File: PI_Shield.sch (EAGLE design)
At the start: 74 parts, among them J10 T2I, J11 T2I, J12 T2I, J13 DF13-4P-1.25DSA, J14 DF13-4P-1.25DSA, J15 DF13-4P-1.25DSA, J16 T2I5P, Q1 220mA/50V/3.5Ω, Q2 220mA/50V/3.5Ω, Q3 220mA/50V/3.5Ω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

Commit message: General routing complete
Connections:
- removed net DI: U$8.GPIO6
- removed net DI3: U$8.GPIO21
- new net 3VO_1: U$4.3VO
- new net 3VO_2: U$5.3VO
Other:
- moved on the sheet: C13
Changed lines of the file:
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@@
 <?xml version="1.0" encoding="utf-8"?>
 <!DOCTYPE eagle SYSTEM "eagle.dtd">
-<eagle version="9.6.2">
+<eagle version="9.5.2">
 <drawing>
 <settings>
@@
 <attribute name="VALUE" x="193.04" y="68.58" size="1.778" layer="96"/>
 </instance>
-<instance part="C13" gate="G$1" x="238.76" y="160.02" smashed="yes">
-<attribute name="NAME" x="240.284" y="162.941" size="1.778" layer="95" font="vector"/>
-<attribute name="VALUE" x="240.284" y="157.861" size="1.778" layer="96" font="vector"/>
+<instance part="C13" gate="G$1" x="238.76" y="162.56" smashed="yes">
+<attribute name="NAME" x="240.284" y="165.481" size="1.778" layer="95" font="vector"/>
+<attribute name="VALUE" x="240.284" y="160.401" size="1.778" layer="96" font="vector"/>
 </instance>
 <instance part="J1" gate="G$1" x="236.22" y="66.04" smashed="yes">
@@
 <attribute name="VALUE" x="231.14" y="83.82" size="1.778" layer="96"/>
 </instance>
-<instance part="GND28" gate="1" x="238.76" y="152.4" smashed="yes">
-<attribute name="VALUE" x="236.22" y="149.86" size="1.778" layer="96"/>
+<instance part="GND28" gate="1" x="238.76" y="154.94" smashed="yes">
+<attribute name="VALUE" x="236.22" y="152.4" size="1.778" layer="96"/>
 </instance>
 <instance part="R20" gate="G$1" x="241.3" y="134.62" smashed="yes" rot="MR270">
@@
 <pinref part="C13" gate="G$1" pin="2"/>
 <pinref part="GND28" gate="1" pin="GND"/>
-<wire x1="238.76" y1="154.94" x2="238.76" y2="157.48" width="0.1524" layer="91"/>
+<wire x1="238.76" y1="157.48" x2="238.76" y2="160.02" width="0.1524" layer="91"/>
 </segment>
 <segment>
@@
 <net name="3V3" class="3">
 <segment>
-<wire x1="215.9" y1="157.48" x2="215.9" y2="165.1" width="0.1524" layer="91"/>
-<wire x1="215.9" y1="165.1" x2="215.9" y2="167.64" width="0.1524" layer="91"/>
-<wire x1="238.76" y1="165.1" x2="215.9" y2="165.1" width="0.1524" layer="91"/>
-<junction x="215.9" y="165.1"/>
+<wire x1="215.9" y1="157.48" x2="215.9" y2="167.64" width="0.1524" layer="91"/>
+<label x="215.9" y="170.18" size="1.778" layer="95" xref="yes"/>
+<pinref part="U$5" gate="G$1" pin="VIN"/>
 <pinref part="C13" gate="G$1" pin="1"/>
-<label x="215.9" y="167.64" size="1.778" layer="95" xref="yes"/>
-<pinref part="U$5" gate="G$1" pin="VIN"/>
+<wire x1="215.9" y1="167.64" x2="215.9" y2="170.18" width="0.1524" layer="91"/>
+<wire x1="238.76" y1="167.64" x2="215.9" y2="167.64" width="0.1524" layer="91"/>
+<junction x="215.9" y="167.64"/>
 </segment>
 <segment>
@@
 <wire x1="167.64" y1="139.7" x2="175.26" y2="139.7" width="0.1524" layer="91"/>
 <label x="172.72" y="139.7" size="1.778" layer="95"/>
-</segment>
-</net>
-<net name="DI" class="0">
-<segment>
-<pinref part="U$8" gate="G$1" pin="GPIO6"/>
-<wire x1="53.34" y1="93.98" x2="58.42" y2="93.98" width="0.1524" layer="91"/>
-<label x="58.42" y="93.98" size="1.778" layer="95" xref="yes"/>
 </segment>
 </net>
@@
 </segment>
 </net>
-<net name="DI3" class="0">
-<segment>
-<pinref part="U$8" gate="G$1" pin="GPIO21"/>
-<wire x1="25.4" y1="114.3" x2="20.32" y2="114.3" width="0.1524" layer="91"/>
-<label x="20.32" y="114.3" size="1.778" layer="95" rot="R180" xref="yes"/>
-</segment>
-</net>
 <net name="DI2" class="0">
 <segment>
@@
 </segment>
 </net>
+<net name="3VO_1" class="0">
+<segment>
+<pinref part="U$4" gate="G$1" pin="3VO"/>
+<wire x1="167.64" y1="149.86" x2="175.26" y2="149.86" width="0.1524" layer="91"/>
+<label x="172.72" y="149.86" size="1.778" layer="95"/>
+</segment>
+</net>
+<net name="3VO_2" class="0">
+<segment>
+<pinref part="U$5" gate="G$1" pin="3VO"/>
+<wire x1="231.14" y1="149.86" x2="238.76" y2="149.86" width="0.1524" layer="91"/>
+<label x="233.68" y="149.86" size="1.778" layer="95"/>
+</segment>
+</net>

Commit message: labels, routing touch ups, etc
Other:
- note removed: "CONNECT INTERRUPT PINS FROM CONTROLLER TO PI?"
- moved on the sheet: Q2
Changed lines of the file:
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@@
 <?xml version="1.0" encoding="utf-8"?>
 <!DOCTYPE eagle SYSTEM "eagle.dtd">
-<eagle version="9.5.2">
+<eagle version="9.6.2">
 <drawing>
 <settings>
@@
 Silent mode is unwanted
 Do not populate R3</text>
-<text x="-73.66" y="147.32" size="1.778" layer="91">CONNECT INTERRUPT PINS FROM CONTROLLER TO PI?</text>
 </plain>
 <instances>
@@
 <pinref part="U$1" gate="G$1" pin="RX0BF"/>
 <wire x1="60.96" y1="129.54" x2="63.5" y2="129.54" width="0.1524" layer="91"/>
-<label x="63.5" y="129.54" size="1.778" layer="95"/>
+<label x="63.5" y="129.54" size="1.27" layer="95" xref="yes"/>
 </segment>
 </net>
@@
 <pinref part="U$1" gate="G$1" pin="RX1BF"/>
 <wire x1="60.96" y1="127" x2="63.5" y2="127" width="0.1524" layer="91"/>
-<label x="63.5" y="127" size="1.778" layer="95"/>
+<label x="63.5" y="127" size="1.27" layer="95" xref="yes"/>
 </segment>
 </net>
@@
 <attribute name="VALUE" x="62.484" y="38.1" size="1.778" layer="96" font="vector" rot="R90" align="top-center"/>
 </instance>
-<instance part="Q2" gate="NMOS" x="78.74" y="27.94" smashed="yes" rot="R90">
-<attribute name="NAME" x="78.74" y="33.02" size="1.778" layer="95" font="vector" rot="R90"/>
-<attribute name="VALUE" x="81.28" y="33.02" size="1.778" layer="96" font="vector" rot="R90"/>
+<instance part="Q2" gate="NMOS" x="63.5" y="22.86" smashed="yes" rot="MR0">
+<attribute name="NAME" x="58.42" y="22.86" size="1.778" layer="95" font="vector" rot="MR0"/>
+<attribute name="VALUE" x="58.42" y="20.32" size="1.778" layer="96" font="vector" rot="MR0"/>
 </instance>
 <instance part="R25" gate="G$1" x="111.76" y="43.18" smashed="yes" rot="R270">
@@
 <segment>
 <pinref part="Q2" gate="NMOS" pin="S"/>
-<wire x1="83.82" y1="30.48" x2="88.9" y2="30.48" width="0.1524" layer="91"/>
-<label x="86.36" y="30.48" size="1.778" layer="95"/>
+<wire x1="60.96" y1="17.78" x2="60.96" y2="12.7" width="0.1524" layer="91"/>
+<label x="60.96" y="12.7" size="1.778" layer="95"/>
 </segment>
 <segment>
@@
 <segment>
 <pinref part="R24" gate="G$1" pin="1"/>
-<wire x1="60.96" y1="33.02" x2="60.96" y2="30.48" width="0.1524" layer="91"/>
 <pinref part="Q2" gate="NMOS" pin="D"/>
-<wire x1="60.96" y1="30.48" x2="73.66" y2="30.48" width="0.1524" layer="91"/>
+<wire x1="60.96" y1="33.02" x2="60.96" y2="27.94" width="0.1524" layer="91"/>
 </segment>
 </net>
@@
 <label x="114.3" y="33.02" size="1.778" layer="95"/>
 <pinref part="Q2" gate="NMOS" pin="G"/>
-<wire x1="81.28" y1="22.86" x2="81.28" y2="20.32" width="0.1524" layer="91"/>
-<wire x1="81.28" y1="20.32" x2="99.06" y2="20.32" width="0.1524" layer="91"/>
+<wire x1="68.58" y1="20.32" x2="99.06" y2="20.32" width="0.1524" layer="91"/>
 <wire x1="99.06" y1="20.32" x2="99.06" y2="33.02" width="0.1524" layer="91"/>
 <wire x1="99.06" y1="33.02" x2="111.76" y2="33.02" width="0.1524" layer="91"/>

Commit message: Finishing touches
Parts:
- added D3, D5: (no value), SparkFun-LED:LED0603
- added R26, R27: RESISTOR0603, SparkFun-Resistors:RESISTOR0603
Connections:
- net CAN_N renamed CAN_L
- net CAN_P renamed CAN_H
- new net N$12: D5.A, R27.1
- new net N$9: D3.A, R26.1
- net 3V3: now also R27.2
- net 5V: now also R26.2
- net GND: now also D3.C, D5.C
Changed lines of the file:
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@@
 <?xml version="1.0" encoding="utf-8"?>
 <!DOCTYPE eagle SYSTEM "eagle.dtd">
-<eagle version="9.6.2">
+<eagle version="9.5.2">
 <drawing>
 <settings>
@@
 <class number="2" name="5V" width="0.508" drill="0">
 </class>
-<class number="3" name="3.3V" width="0.6096" drill="0">
+<class number="3" name="3.3V" width="0.508" drill="0">
 </class>
 </classes>
@@
 <part name="GND46" library="supply1" library_urn="urn:adsk.eagle:library:371" deviceset="GND" device=""/>
 <part name="GND47" library="supply1" library_urn="urn:adsk.eagle:library:371" deviceset="GND" device=""/>
+<part name="R26" library="SparkFun-Resistors" library_urn="urn:adsk.eagle:library:532" deviceset="RESISTOR" device="0603" package3d_urn="urn:adsk.eagle:package:39650/1" value=""/>
+<part name="R27" library="SparkFun-Resistors" library_urn="urn:adsk.eagle:library:532" deviceset="RESISTOR" device="0603" package3d_urn="urn:adsk.eagle:package:39650/1" value=""/>
+<part name="D3" library="SparkFun-LED" library_urn="urn:adsk.eagle:library:529" deviceset="LED" device="0603" package3d_urn="urn:adsk.eagle:package:39354/1"/>
+<part name="D5" library="SparkFun-LED" library_urn="urn:adsk.eagle:library:529" deviceset="LED" device="0603" package3d_urn="urn:adsk.eagle:package:39354/1"/>
 </parts>
 <sheets>
@@
 </segment>
 </net>
-<net name="CAN_P" class="1">
+<net name="CAN_H" class="1">
 <segment>
 <pinref part="R6" gate="G$1" pin="2"/>
@@
 </segment>
 </net>
-<net name="CAN_N" class="1">
+<net name="CAN_L" class="1">
 <segment>
 <pinref part="R7" gate="G$1" pin="1"/>
@@
 </segment>
 </net>
-<net name="CAN_P" class="1">
+<net name="CAN_H" class="1">
 <segment>
 <pinref part="J5" gate="G$1" pin="2"/>
@@
 </segment>
 </net>
-<net name="CAN_N" class="1">
+<net name="CAN_L" class="1">
 <segment>
 <pinref part="J5" gate="G$1" pin="1"/>
@@
 </instance>
 <instance part="U$6" gate="G$1" x="111.76" y="22.86" smashed="yes" rot="R270"/>
+<instance part="R26" gate="G$1" x="12.7" y="30.48" smashed="yes" rot="R90">
+<attribute name="NAME" x="11.176" y="30.48" size="1.778" layer="95" font="vector" rot="R90" align="bottom-center"/>
+<attribute name="VALUE" x="14.224" y="30.48" size="1.778" layer="96" font="vector" rot="R90" align="top-center"/>
+</instance>
+<instance part="R27" gate="G$1" x="22.86" y="30.48" smashed="yes" rot="R90">
+<attribute name="NAME" x="21.336" y="30.48" size="1.778" layer="95" font="vector" rot="R90" align="bottom-center"/>
+<attribute name="VALUE" x="24.384" y="30.48" size="1.778" layer="96" font="vector" rot="R90" align="top-center"/>
+</instance>
+<instance part="D3" gate="G$1" x="12.7" y="17.78" smashed="yes">
+<attribute name="NAME" x="9.271" y="13.208" size="1.778" layer="95" font="vector" rot="R90"/>
+<attribute name="VALUE" x="14.605" y="13.208" size="1.778" layer="96" font="vector" rot="R90" align="top-left"/>
+</instance>
+<instance part="D5" gate="G$1" x="22.86" y="17.78" smashed="yes">
+<attribute name="NAME" x="19.431" y="13.208" size="1.778" layer="95" font="vector" rot="R90"/>
+<attribute name="VALUE" x="24.765" y="13.208" size="1.778" layer="96" font="vector" rot="R90" align="top-left"/>
+</instance>
 </instances>
 <busses>
@@
 <label x="111.76" y="10.16" size="1.778" layer="95"/>
 </segment>
+<segment>
+<pinref part="D3" gate="G$1" pin="C"/>
+<wire x1="12.7" y1="12.7" x2="12.7" y2="10.16" width="0.1524" layer="91"/>
+<label x="12.7" y="7.62" size="1.778" layer="95"/>
+</segment>
+<segment>
+<pinref part="D5" gate="G$1" pin="C"/>
+<wire x1="22.86" y1="12.7" x2="22.86" y2="10.16" width="0.1524" layer="91"/>
+<label x="22.86" y="7.62" size="1.778" layer="95"/>
+</segment>
 </net>
 <net name="5V" class="2">
@@
 <label x="170.18" y="83.82" size="1.778" layer="95"/>
 </segment>
+<segment>
+<pinref part="R26" gate="G$1" pin="2"/>
+<wire x1="12.7" y1="35.56" x2="12.7" y2="38.1" width="0.1524" layer="91"/>
+<label x="12.7" y="38.1" size="1.778" layer="95"/>
+</segment>
 </net>
 <net name="SDA" class="0">
@@
 <wire x1="111.76" y1="48.26" x2="111.76" y2="53.34" width="0.1524" layer="91"/>
 <label x="109.22" y="53.34" size="1.778" layer="95"/>
+</segment>
+<segment>
+<pinref part="R27" gate="G$1" pin="2"/>
+<wire x1="22.86" y1="35.56" x2="22.86" y2="38.1" width="0.1524" layer="91"/>
+<label x="22.86" y="38.1" size="1.778" layer="95"/>
 </segment>
 </net>
@@
 </segment>
 </net>
+<net name="N$9" class="0">
+<segment>
+<pinref part="D3" gate="G$1" pin="A"/>
+<pinref part="R26" gate="G$1" pin="1"/>
+<wire x1="12.7" y1="20.32" x2="12.7" y2="25.4" width="0.1524" layer="91"/>
+</segment>
+</net>
+<net name="N$12" class="0">
+<segment>
+<pinref part="D5" gate="G$1" pin="A"/>
+<pinref part="R27" gate="G$1" pin="1"/>
+<wire x1="22.86" y1="20.32" x2="22.86" y2="25.4" width="0.1524" layer="91"/>
+</segment>
+</net>

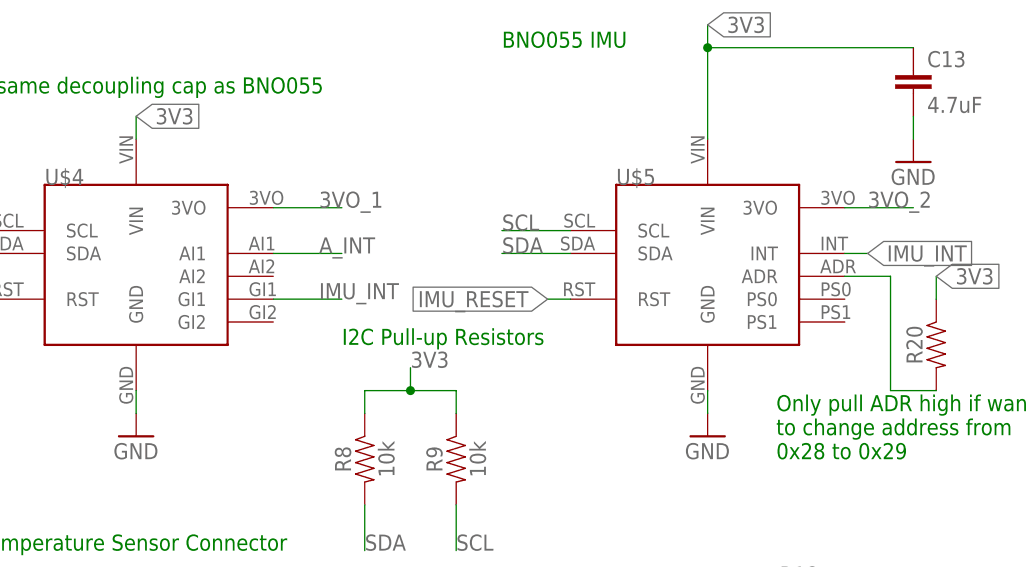
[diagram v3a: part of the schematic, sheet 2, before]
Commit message: Ordering text, step, and pdf
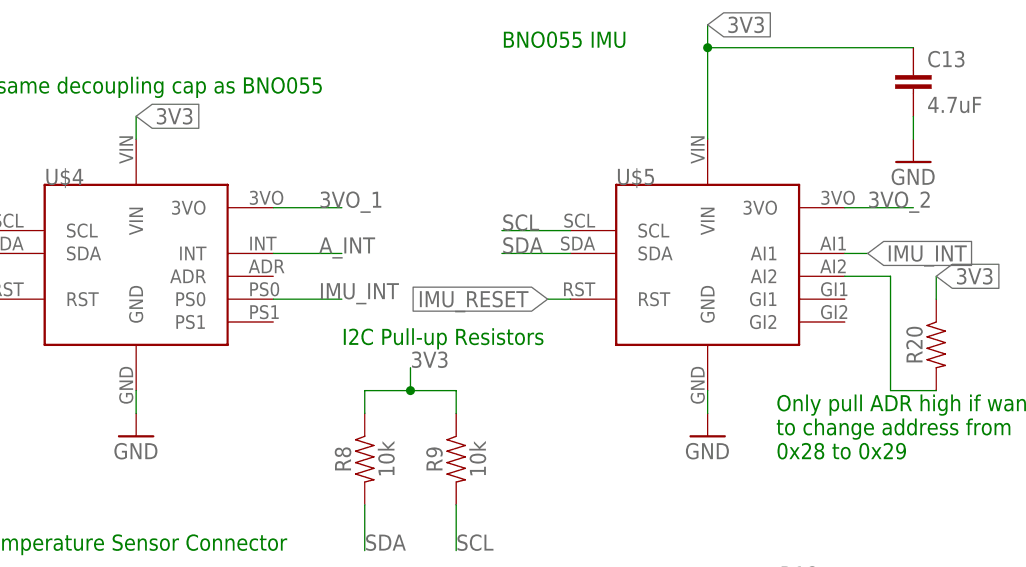
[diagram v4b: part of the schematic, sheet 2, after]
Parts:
- U$4: value ADAFRUIT-FXOS8700-FXAS21002 -> ADAFRUIT-BNO055; device Adafruit IMUs - BNO055 and FX:ADAFRUIT-FXOS8700-FXAS21002 -> Adafruit IMUs - BNO055 and FX:ADAFRUIT-BNO055
- U$5: value ADAFRUIT-BNO055 -> ADAFRUIT-FXOS8700-FXAS21002; device Adafruit IMUs - BNO055 and FX:ADAFRUIT-BNO055 -> Adafruit IMUs - BNO055 and FX:ADAFRUIT-FXOS8700-FXAS21002
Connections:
- net A_INT: now also U$4.INT; no longer U$4.AI1
- net IMU_INT: now also U$4.PS0, U$5.AI1; no longer U$4.GI1, U$5.INT
- net N$1: now also U$5.AI2; no longer U$5.ADR
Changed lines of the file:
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@@
 <?xml version="1.0" encoding="utf-8"?>
 <!DOCTYPE eagle SYSTEM "eagle.dtd">
-<eagle version="9.5.2">
+<eagle version="9.6.2">
 <drawing>
 <settings>
@@
 </classes>
 <parts>
-<part name="FRAME1" library="frames" library_urn="urn:adsk.eagle:library:229" deviceset="A4L-LOC" device=""/>
 <part name="Y1" library="ECS-80-S-4X" deviceset="ECS-80-S-4X" device=""/>
 <part name="GND1" library="supply1" library_urn="urn:adsk.eagle:library:371" deviceset="GND" device=""/>
-<part name="FRAME2" library="frames" library_urn="urn:adsk.eagle:library:229" deviceset="A4L-LOC" device=""/>
-<part name="FRAME3" library="frames" library_urn="urn:adsk.eagle:library:229" deviceset="A4L-LOC" device=""/>
 <part name="R6" library="SparkFun-Resistors" library_urn="urn:adsk.eagle:library:532" deviceset="RESISTOR" device="0603" package3d_urn="urn:adsk.eagle:package:39650/1" value="60"/>
 <part name="R7" library="SparkFun-Resistors" library_urn="urn:adsk.eagle:library:532" deviceset="RESISTOR" device="0603" package3d_urn="urn:adsk.eagle:package:39650/1" value="60"/>
@@
 <part name="GND28" library="supply1" library_urn="urn:adsk.eagle:library:371" deviceset="GND" device=""/>
 <part name="R20" library="SparkFun-Resistors" library_urn="urn:adsk.eagle:library:532" deviceset="RESISTOR" device="0603" package3d_urn="urn:adsk.eagle:package:39650/1" value=""/>
-<part name="U$4" library="Adafruit IMUs - BNO055 and FX" deviceset="ADAFRUIT-FXOS8700-FXAS21002" device=""/>
-<part name="U$5" library="Adafruit IMUs - BNO055 and FX" deviceset="ADAFRUIT-BNO055" device=""/>
+<part name="U$4" library="Adafruit IMUs - BNO055 and FX" deviceset="ADAFRUIT-BNO055" device=""/>
+<part name="U$5" library="Adafruit IMUs - BNO055 and FX" deviceset="ADAFRUIT-FXOS8700-FXAS21002" device=""/>
 <part name="GND31" library="supply1" library_urn="urn:adsk.eagle:library:371" deviceset="GND" device=""/>
 <part name="U$3" library="usb conn" deviceset="USB-MICRO" device=""/>
@@
 <part name="D3" library="SparkFun-LED" library_urn="urn:adsk.eagle:library:529" deviceset="LED" device="0603" package3d_urn="urn:adsk.eagle:package:39354/1"/>
 <part name="D5" library="SparkFun-LED" library_urn="urn:adsk.eagle:library:529" deviceset="LED" device="0603" package3d_urn="urn:adsk.eagle:package:39354/1"/>
+<part name="FRAME4" library="SparkFun-Aesthetics" library_urn="urn:adsk.eagle:library:507" deviceset="FRAME-A4L" device=""/>
+<part name="FRAME1" library="SparkFun-Aesthetics" library_urn="urn:adsk.eagle:library:507" deviceset="FRAME-A4L" device=""/>
+<part name="FRAME2" library="SparkFun-Aesthetics" library_urn="urn:adsk.eagle:library:507" deviceset="FRAME-A4L" device=""/>
 </parts>
 <sheets>
@@
 </plain>
 <instances>
-<instance part="FRAME1" gate="G$1" x="0" y="0" smashed="yes">
-<attribute name="DRAWING_NAME" x="217.17" y="15.24" size="2.54" layer="94"/>
-<attribute name="LAST_DATE_TIME" x="217.17" y="10.16" size="2.286" layer="94"/>
-<attribute name="SHEET" x="230.505" y="5.08" size="2.54" layer="94"/>
-</instance>
 <instance part="Y1" gate="G$1" x="20.32" y="48.26" smashed="yes" rot="R180">
 <attribute name="NAME" x="24.89693125" y="45.971540625" size="1.77991875" layer="95" rot="R180"/>
@@
 <attribute name="NAME" x="29.464" y="41.021" size="1.778" layer="95" font="vector"/>
 <attribute name="VALUE" x="29.464" y="35.941" size="1.778" layer="96" font="vector"/>
+</instance>
+<instance part="FRAME4" gate="G$1" x="0" y="0" smashed="yes">
+<attribute name="DRAWING_NAME" x="181.61" y="11.43" size="2.54" layer="94" font="vector"/>
+<attribute name="LAST_DATE_TIME" x="181.61" y="6.35" size="2.286" layer="94" font="vector"/>
+<attribute name="SHEET" x="195.58" y="1.27" size="2.54" layer="94" font="vector"/>
 </instance>
 </instances>
@@
 </plain>
 <instances>
-<instance part="FRAME2" gate="G$1" x="0" y="0" smashed="yes">
-<attribute name="DRAWING_NAME" x="217.17" y="15.24" size="2.54" layer="94"/>
-<attribute name="LAST_DATE_TIME" x="217.17" y="10.16" size="2.286" layer="94"/>
-<attribute name="SHEET" x="230.505" y="5.08" size="2.54" layer="94"/>
-</instance>
 <instance part="J4" gate="G$1" x="182.88" y="38.1" smashed="yes">
 <attribute name="VALUE" x="180.34" y="28.194" size="1.778" layer="96" font="vector"/>
@@
 <instance part="GND47" gate="1" x="66.04" y="38.1" smashed="yes" rot="R90">
 <attribute name="VALUE" x="68.58" y="35.56" size="1.778" layer="96" rot="R90"/>
+</instance>
+<instance part="FRAME2" gate="G$1" x="0" y="0" smashed="yes">
+<attribute name="DRAWING_NAME" x="181.61" y="11.43" size="2.54" layer="94" font="vector"/>
+<attribute name="LAST_DATE_TIME" x="181.61" y="6.35" size="2.286" layer="94" font="vector"/>
+<attribute name="SHEET" x="195.58" y="1.27" size="2.54" layer="94" font="vector"/>
 </instance>
 </instances>
@@
 <label x="233.68" y="144.78" size="1.778" layer="95" xref="yes"/>
 <wire x1="231.14" y1="144.78" x2="233.68" y2="144.78" width="0.1524" layer="91"/>
-<pinref part="U$5" gate="G$1" pin="INT"/>
+<pinref part="U$5" gate="G$1" pin="AI1"/>
 </segment>
 <segment>
@@
 </segment>
 <segment>
-<pinref part="U$4" gate="G$1" pin="GI1"/>
+<pinref part="U$4" gate="G$1" pin="PS0"/>
 <wire x1="167.64" y1="139.7" x2="175.26" y2="139.7" width="0.1524" layer="91"/>
 <label x="172.72" y="139.7" size="1.778" layer="95"/>
@@
 <wire x1="236.22" y1="129.54" x2="241.3" y2="129.54" width="0.1524" layer="91"/>
 <pinref part="R20" gate="G$1" pin="2"/>
-<pinref part="U$5" gate="G$1" pin="ADR"/>
+<pinref part="U$5" gate="G$1" pin="AI2"/>
 </segment>
 </net>
@@
 <net name="A_INT" class="0">
 <segment>
-<pinref part="U$4" gate="G$1" pin="AI1"/>
+<pinref part="U$4" gate="G$1" pin="INT"/>
 <wire x1="167.64" y1="144.78" x2="175.26" y2="144.78" width="0.1524" layer="91"/>
 <label x="172.72" y="144.78" size="1.778" layer="95"/>
@@
 </plain>
 <instances>
-<instance part="FRAME3" gate="G$1" x="0" y="0" smashed="yes">
-<attribute name="DRAWING_NAME" x="217.17" y="15.24" size="2.54" layer="94"/>
-<attribute name="LAST_DATE_TIME" x="217.17" y="10.16" size="2.286" layer="94"/>
-<attribute name="SHEET" x="230.505" y="5.08" size="2.54" layer="94"/>
-</instance>
 <instance part="U1" gate="A" x="127" y="144.78" smashed="yes">
 <attribute name="NAME" x="155.3306" y="153.90988125" size="2.08538125" layer="95" ratio="6" rot="SR0"/>
@@
 <attribute name="VALUE" x="24.765" y="13.208" size="1.778" layer="96" font="vector" rot="R90" align="top-left"/>
 </instance>
+<instance part="FRAME1" gate="G$1" x="0" y="0" smashed="yes">
+<attribute name="DRAWING_NAME" x="181.61" y="11.43" size="2.54" layer="94" font="vector"/>
+<attribute name="LAST_DATE_TIME" x="181.61" y="6.35" size="2.286" layer="94" font="vector"/>
+<attribute name="SHEET" x="195.58" y="1.27" size="2.54" layer="94" font="vector"/>
+</instance>
 </instances>
